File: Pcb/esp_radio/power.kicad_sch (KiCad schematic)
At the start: 21 parts, among them J1 Power 10V, U1 AMS1117-3.3, U2 AMS1117-5

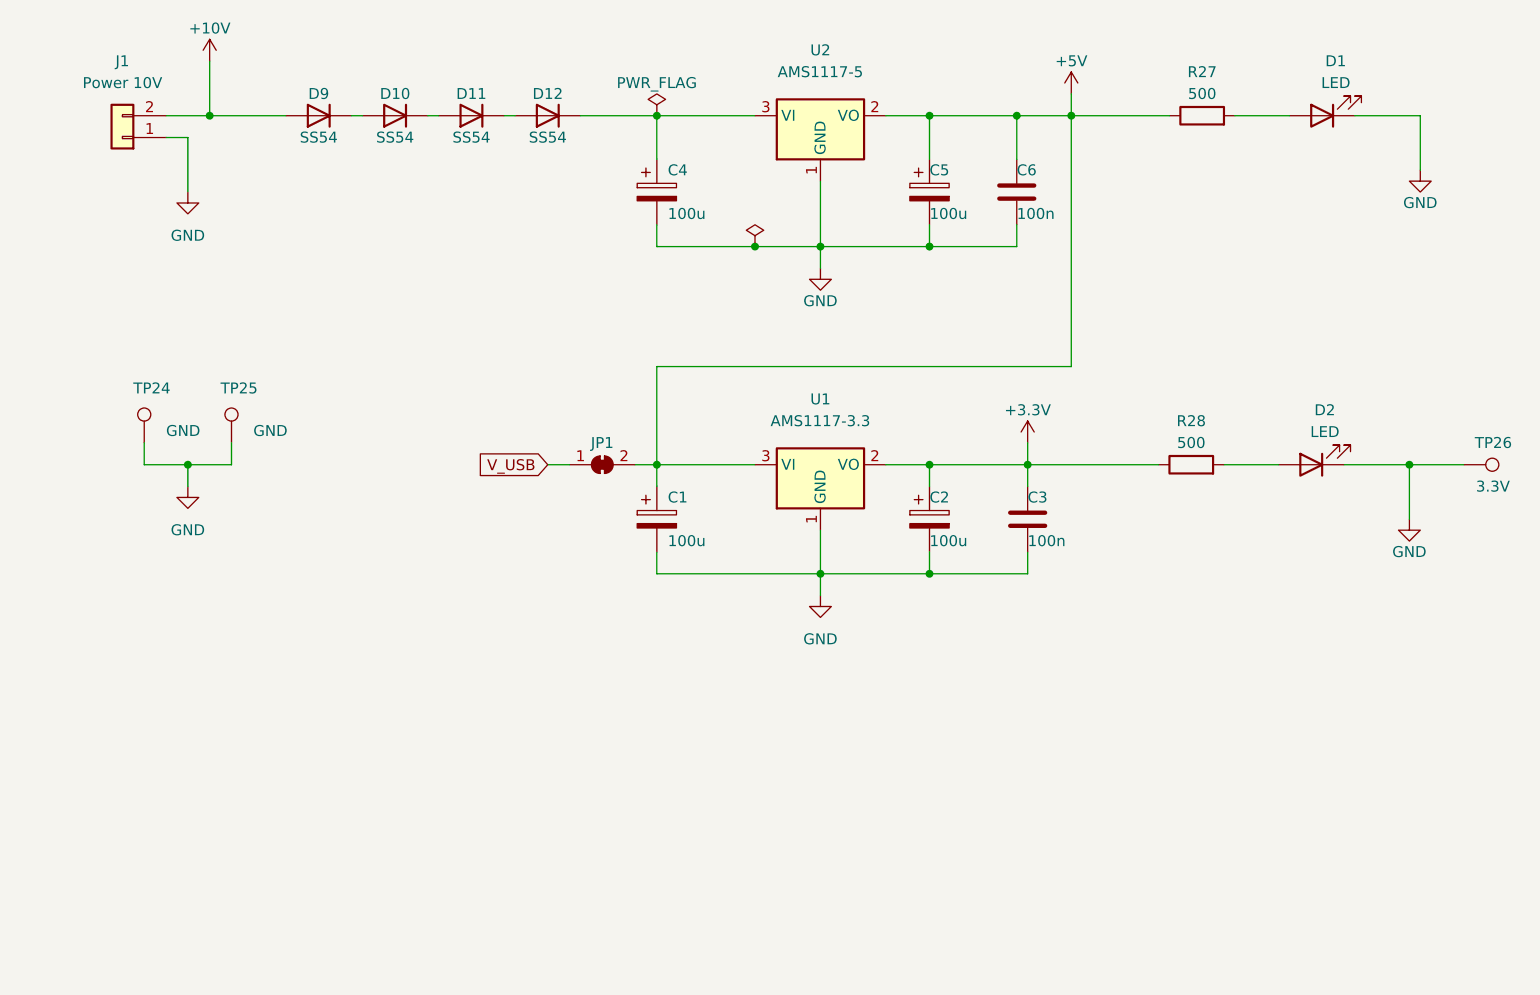
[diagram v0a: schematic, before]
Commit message: Move custom components to kicad_common_library.
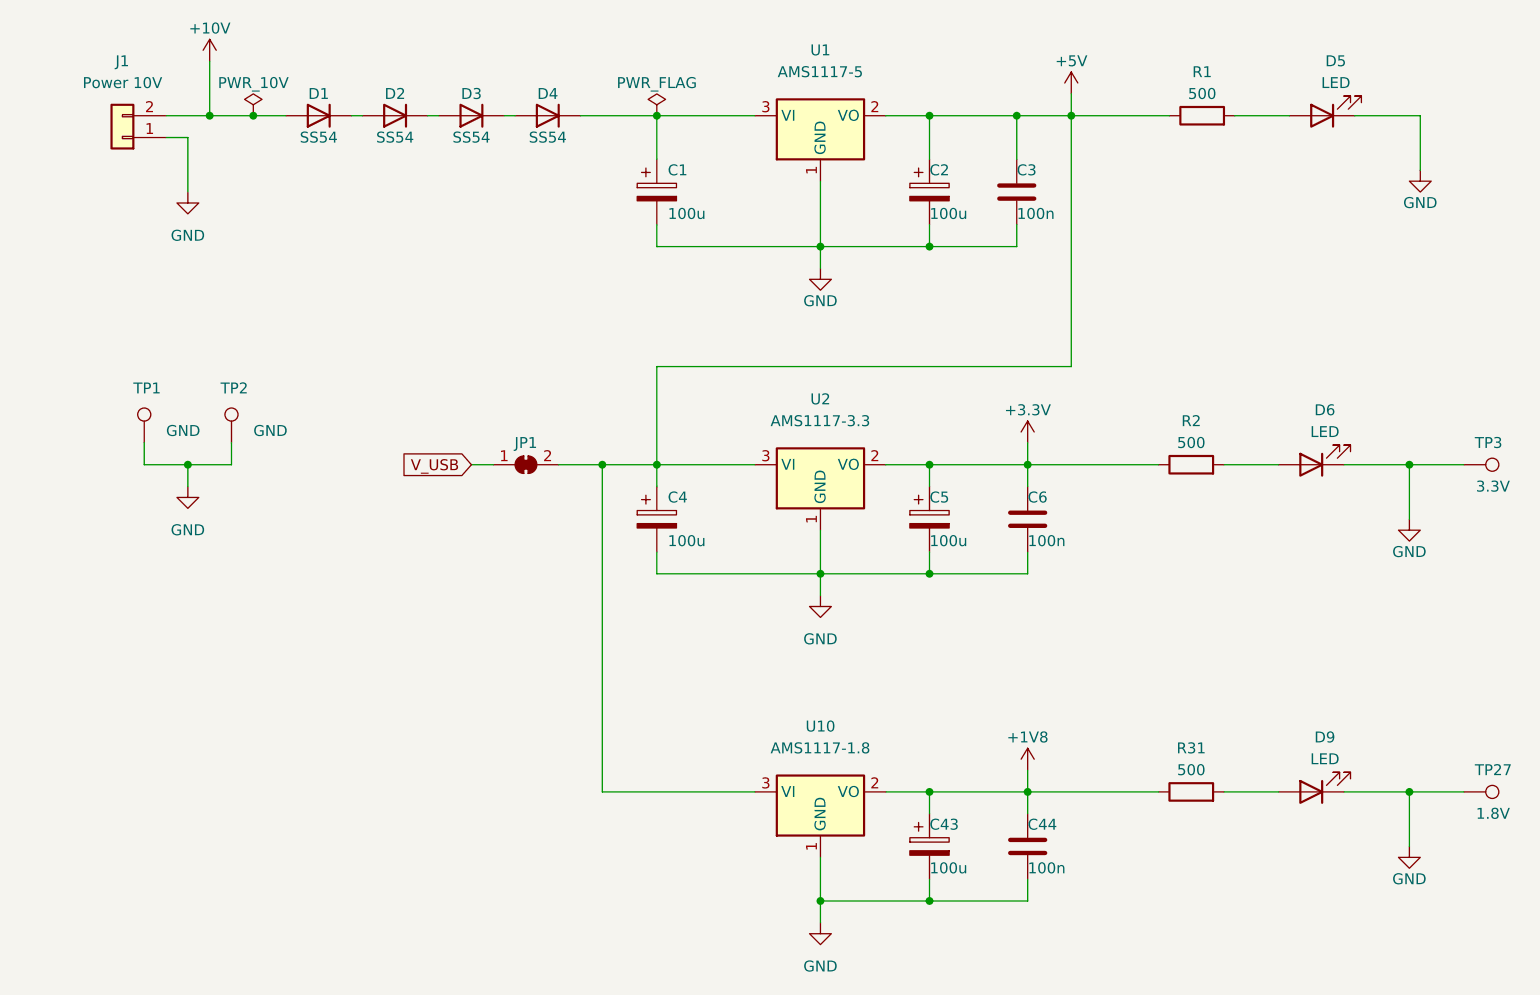
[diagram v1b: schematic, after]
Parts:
- added C43: 100u, Capacitor_THT:CP_Radial_D5.0mm_P2.50mm, symbol Device:C_Polarized
- added C44: 100n, kicad_common_lib:C_0805, symbol Device:C
- added D9: LED, symbol Device:LED
- added R31: 500, symbol Device:R
- added TP27: 1.8V, symbol Connector:TestPoint
- added U10: AMS1117-1.8, Package_TO_SOT_SMD:SOT-223-3_TabPin2, symbol Regulator_Linear:AMS1117-1.8
- renumbered C4 to C1, C5 to C2, C6 to C3, C1 to C4, C2 to C5, C3 to C6, D9 to D1, D10 to D2, D11 to D3, D12 to D4, D1 to D5, D2 to D6, R27 to R1, R28 to R2, TP24 to TP1, TP25 to TP2, TP26 to TP3, U2 to U1, U1 to U2
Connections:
- net +5V: now also U10.3 (VI)
- net GND: now also C43.2, C44.2, D9.1 (K), TP27.1, U10.1 (GND)
- new net: D9.2 (A), R31.2
- new net +1V8: C43.1, C44.1, R31.1, U10.2 (VO)
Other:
- moved on the sheet: JP1

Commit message: Add components layout on PCB
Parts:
- D1, D2, D3, D4: footprint (none) -> Diode_SMD:D_SMB_Handsoldering
- D5, D6, D9: footprint (none) -> LED_SMD:LED_1210_3225Metric_Pad1.42x2.65mm_HandSolder
- J1: footprint (none) -> Connector_JST:JST_XH_S2B-XH-A_1x02_P2.50mm_Horizontal
- R1, R2, R31: footprint (none) -> kicad_common_lib:R_0805
- TP1, TP2, TP27, TP3: footprint (none) -> TestPoint:TestPoint_THTPad_D2.0mm_Drill1.0mm
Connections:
- net +1V8: now also TP27.1
- net +3.3V: now also TP3.1
- net GND: no longer TP27.1, TP3.1
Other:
- moved on the sheet: R2, R31

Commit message: Finish board routing
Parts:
- added C45: 100n, kicad_common_lib:C_0805, symbol Device:C
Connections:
- net +10V: now also C45.1
- net GND: now also C45.2
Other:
- moved on the sheet: J1
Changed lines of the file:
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@@
+    (stroke (width 0) (type default))
+  )
+  (wire (pts (xy 41.91 49.53) (xy 41.91 54.61))
     (stroke (width 0) (type default))
   )
@@
     (stroke (width 0) (type default))
   )
-  (wire (pts (xy 34.29 39.37) (xy 34.29 45.72))
+  (wire (pts (xy 29.21 39.37) (xy 29.21 45.72))
     (stroke (width 0) (type solid))
   )
@@
     (stroke (width 0) (type default))
   )
-  (wire (pts (xy 31.75 36.83) (xy 36.83 36.83))
+  (wire (pts (xy 25.4 36.83) (xy 36.83 36.83))
     (stroke (width 0) (type default))
   )
@@
     (stroke (width 0) (type default))
   )
+  (wire (pts (xy 41.91 36.83) (xy 41.91 41.91))
+    (stroke (width 0) (type default))
+  )
   (wire (pts (xy 39.37 77.47) (xy 39.37 74.93))
     (stroke (width 0) (type default))
@@
     (stroke (width 0) (type default))
   )
-  (wire (pts (xy 31.75 39.37) (xy 34.29 39.37))
+  (wire (pts (xy 25.4 39.37) (xy 29.21 39.37))
     (stroke (width 0) (type solid))
   )
@@
     )
   )
+  (symbol (lib_id "power:GND") (at 41.91 54.61 0) (unit 1)
+    (in_bom yes) (on_board yes) (dnp no) (fields_autoplaced)
+    (property "Reference" "#PWR073" (at 41.91 60.96 0)
+      (effects (font (size 1.27 1.27)) hide)
+    )
+    (property "Value" "GND" (at 41.91 59.69 0)
+      (effects (font (size 1.27 1.27)))
+    )
+    (property "Footprint" "" (at 41.91 54.61 0)
+      (effects (font (size 1.27 1.27)) hide)
+    )
+    (property "Datasheet" "" (at 41.91 54.61 0)
+      (effects (font (size 1.27 1.27)) hide)
+    )
+    (pin "1")
+    (instances
+      (project "esp_radio"
+        (path "/c9e2e0d2-0655-4f5e-8e13-71b41b1f7cfe/9686c251-96de-4991-9702-894d5bd1468a"
+          (reference "#PWR073") (unit 1)
+        )
+      )
+    )
+  )
   (symbol (lib_id "Device:C_Polarized") (at 120.65 121.92 0) (unit 1)
     (in_bom yes) (on_board yes) (dnp no)
@@
     )
   )
+  (symbol (lib_id "Device:C") (at 41.91 45.72 0) (unit 1)
+    (in_bom yes) (on_board yes) (dnp no)
+    (property "Reference" "C45" (at 41.91 43.18 0)
+      (effects (font (size 1.27 1.27)) (justify left))
+    )
+    (property "Value" "100n" (at 41.91 48.26 0)
+      (effects (font (size 1.27 1.27)) (justify left))
+    )
+    (property "Footprint" "kicad_common_lib:C_0805" (at 42.8752 49.53 0)
+      (effects (font (size 1.27 1.27)) hide)
+    )
+    (property "Datasheet" "~" (at 41.91 45.72 0)
+      (effects (font (size 1.27 1.27)) hide)
+    )
+    (pin "1")
+    (pin "2")
+    (instances
+      (project "esp_radio"
+        (path "/c9e2e0d2-0655-4f5e-8e13-71b41b1f7cfe/9686c251-96de-4991-9702-894d5bd1468a"
+          (reference "C45") (unit 1)
+        )
+      )
+      (project "iot_gateway"
+        (path "/d8268e8f-2c84-4fbb-9908-0fb878740295"
+          (reference "C3") (unit 1)
+        )
+      )
+    )
+  )
   (symbol (lib_id "power:GND") (at 107.95 92.71 0) (unit 1)
     (in_bom yes) (on_board yes) (dnp no) (fields_autoplaced)
@@
     )
   )
-  (symbol (lib_id "power:GND") (at 34.29 45.72 0) (unit 1)
-    (in_bom yes) (on_board yes) (dnp no) (fields_autoplaced)
-    (property "Reference" "#PWR04" (at 34.29 52.07 0)
-      (effects (font (size 1.27 1.27)) hide)
-    )
-    (property "Value" "GND" (at 34.29 50.8 0)
-      (effects (font (size 1.27 1.27)))
-    )
-    (property "Footprint" "" (at 34.29 45.72 0)
-      (effects (font (size 1.27 1.27)) hide)
-    )
-    (property "Datasheet" "" (at 34.29 45.72 0)
+  (symbol (lib_id "power:GND") (at 29.21 45.72 0) (unit 1)
+    (in_bom yes) (on_board yes) (dnp no) (fields_autoplaced)
+    (property "Reference" "#PWR04" (at 29.21 52.07 0)
+      (effects (font (size 1.27 1.27)) hide)
+    )
+    (property "Value" "GND" (at 29.21 50.8 0)
+      (effects (font (size 1.27 1.27)))
+    )
+    (property "Footprint" "" (at 29.21 45.72 0)
+      (effects (font (size 1.27 1.27)) hide)
+    )
+    (property "Datasheet" "" (at 29.21 45.72 0)
       (effects (font (size 1.27 1.27)) hide)
     )
@@
     )
   )
-  (symbol (lib_id "Connector_Generic:Conn_01x02") (at 26.67 39.37 180) (unit 1)
-    (in_bom yes) (on_board yes) (dnp no)
-    (property "Reference" "J1" (at 26.67 30.48 0)
-      (effects (font (size 1.27 1.27)))
-    )
-    (property "Value" "Power 10V" (at 26.67 33.02 0)
-      (effects (font (size 1.27 1.27)))
-    )
-    (property "Footprint" "Connector_JST:JST_XH_S2B-XH-A_1x02_P2.50mm_Horizontal" (at 26.67 39.37 0)
-      (effects (font (size 1.27 1.27)) hide)
-    )
-    (property "Datasheet" "~" (at 26.67 39.37 0)
-      (effects (font (size 1.27 1.27)) hide)
-    )
+  (symbol (lib_id "Connector_Generic:Conn_01x02") (at 20.32 39.37 180) (unit 1)
+    (in_bom yes) (on_board yes) (dnp no)
+    (property "Reference" "J1" (at 20.32 30.48 0)
+      (effects (font (size 1.27 1.27)))
+    )
+    (property "Value" "Power 10V" (at 20.32 33.02 0)
+      (effects (font (size 1.27 1.27)))
+    )
+    (property "Footprint" "Connector_JST:JST_XH_S2B-XH-A_1x02_P2.50mm_Horizontal" (at 20.32 39.37 0)
+      (effects (font (size 1.27 1.27)) hide)
+    )
+    (property "Datasheet" "~" (at 20.32 39.37 0)
+      (effects (font (size 1.27 1.27)) hide)
+    )
